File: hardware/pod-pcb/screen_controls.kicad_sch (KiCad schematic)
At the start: 0 parts

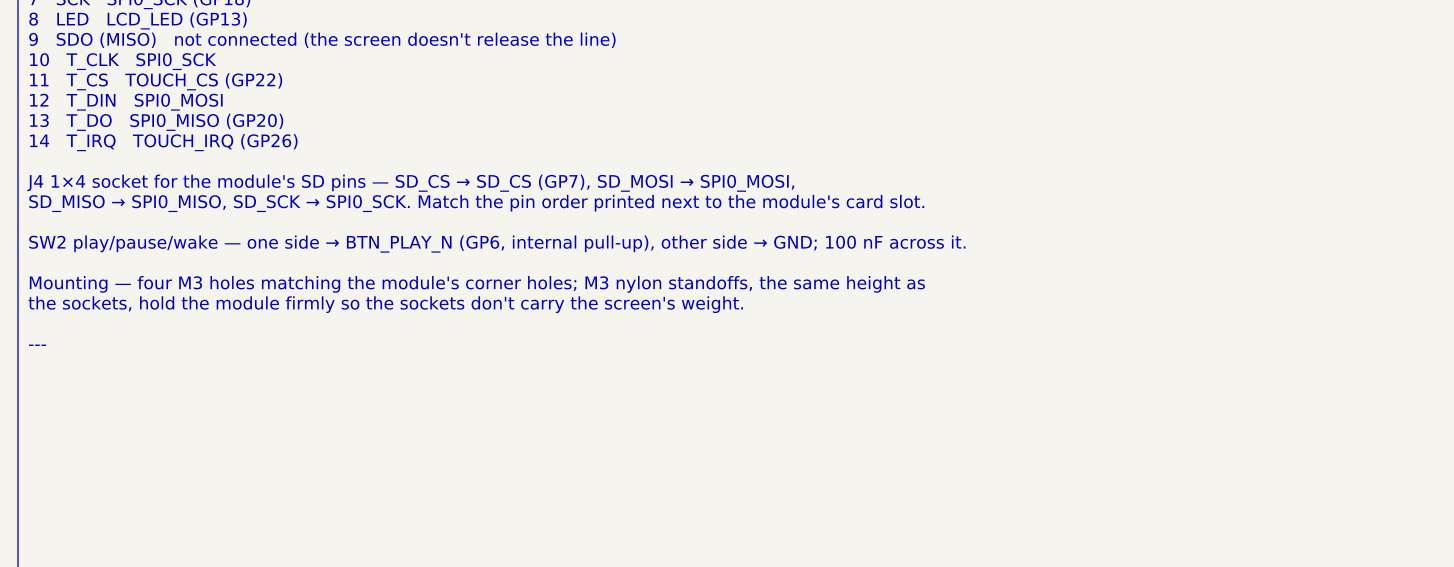
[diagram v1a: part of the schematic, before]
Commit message: PCB: battery moves to the underside of the board
The screen module's microSD holder occupies the gap under the module,
so the 1000 mAh cell no longer fits beside it. It now sits on the
underside of our board (one-sided assembly, no parts on the bottom),
with its lead through a notch to J2. Pod is about 55 x 100 x 24 mm.
Layout, case and progress notes updated; battery outline on B.Fab.

Co-Authored-By: Claude Opus 5.5 <noreply@anthropic.com>
Claude-Session: https://claude.ai/code/session_01DRxt8QzQ72ypvJY6iWLH7J
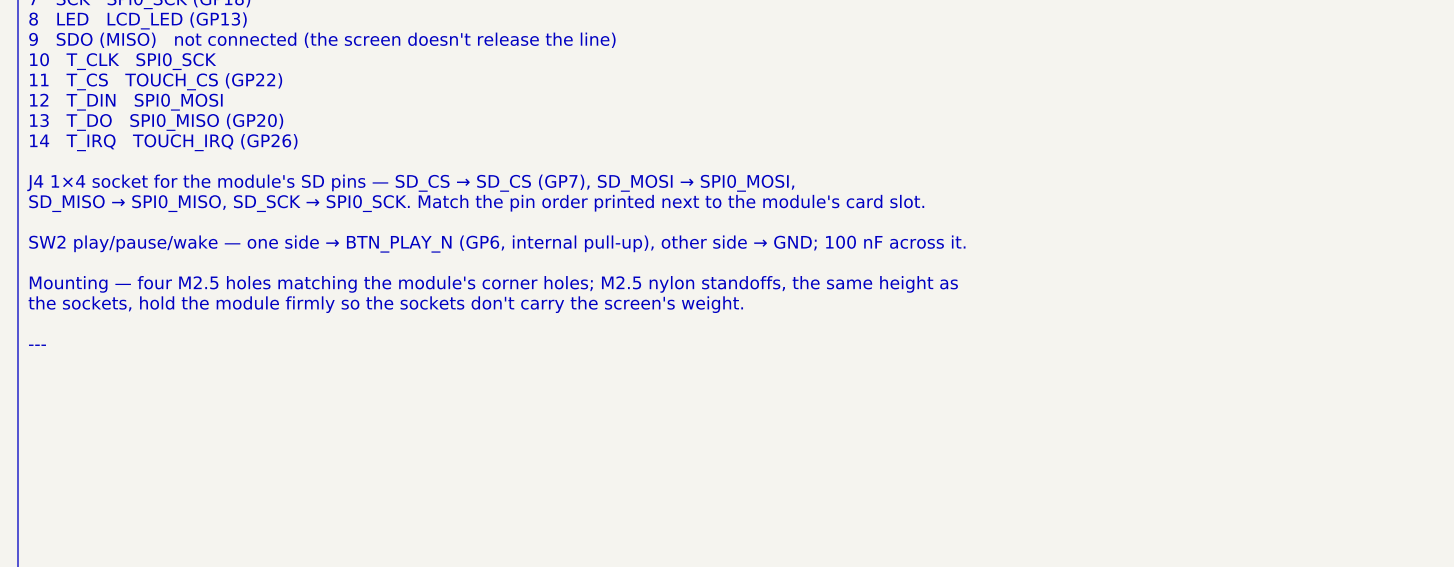
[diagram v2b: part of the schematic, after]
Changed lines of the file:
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@@
     (comment 2 "Spec: docs/pcb-plan.md")
   )
-  (text_box "CHECKLIST — Sheet 5 — Screen sockets\n\nJ3 1×14 socket for the red module (pin order as printed on the module, left to right):\n\nJ3 pin   Module   Net\n1   VCC   3V3\n2   GND   GND\n3   CS   LCD_CS (GP17)\n4   RESET   LCD_RST (GP21)\n5   DC   LCD_DC (GP16)\n6   SDI (MOSI)   SPI0_MOSI (GP19)\n7   SCK   SPI0_SCK (GP18)\n8   LED   LCD_LED (GP13)\n9   SDO (MISO)   not connected (the screen doesn't release the line)\n10   T_CLK   SPI0_SCK\n11   T_CS   TOUCH_CS (GP22)\n12   T_DIN   SPI0_MOSI\n13   T_DO   SPI0_MISO (GP20)\n14   T_IRQ   TOUCH_IRQ (GP26)\n\nJ4 1×4 socket for the module's SD pins — SD_CS → SD_CS (GP7), SD_MOSI → SPI0_MOSI,\nSD_MISO → SPI0_MISO, SD_SCK → SPI0_SCK. Match the pin order printed next to the module's card slot.\n\nSW2 play/pause/wake — one side → BTN_PLAY_N (GP6, internal pull-up), other side → GND; 100 nF across it.\n\nMounting — four M3 holes matching the module's corner holes; M3 nylon standoffs, the same height as\nthe sockets, hold the module firmly so the sockets don't carry the screen's weight.\n\n---"
+  (text_box "CHECKLIST — Sheet 5 — Screen sockets\n\nJ3 1×14 socket for the red module (pin order as printed on the module, left to right):\n\nJ3 pin   Module   Net\n1   VCC   3V3\n2   GND   GND\n3   CS   LCD_CS (GP17)\n4   RESET   LCD_RST (GP21)\n5   DC   LCD_DC (GP16)\n6   SDI (MOSI)   SPI0_MOSI (GP19)\n7   SCK   SPI0_SCK (GP18)\n8   LED   LCD_LED (GP13)\n9   SDO (MISO)   not connected (the screen doesn't release the line)\n10   T_CLK   SPI0_SCK\n11   T_CS   TOUCH_CS (GP22)\n12   T_DIN   SPI0_MOSI\n13   T_DO   SPI0_MISO (GP20)\n14   T_IRQ   TOUCH_IRQ (GP26)\n\nJ4 1×4 socket for the module's SD pins — SD_CS → SD_CS (GP7), SD_MOSI → SPI0_MOSI,\nSD_MISO → SPI0_MISO, SD_SCK → SPI0_SCK. Match the pin order printed next to the module's card slot.\n\nSW2 play/pause/wake — one side → BTN_PLAY_N (GP6, internal pull-up), other side → GND; 100 nF across it.\n\nMounting — four M2.5 holes matching the module's corner holes; M2.5 nylon standoffs, the same height as\nthe sockets, hold the module firmly so the sockets don't carry the screen's weight.\n\n---"
     (at 15 20 0) (size 390 255)
     (stroke (width 0) (type default))
